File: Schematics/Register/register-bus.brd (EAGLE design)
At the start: 119.4 x 70.8 mm, 17 parts

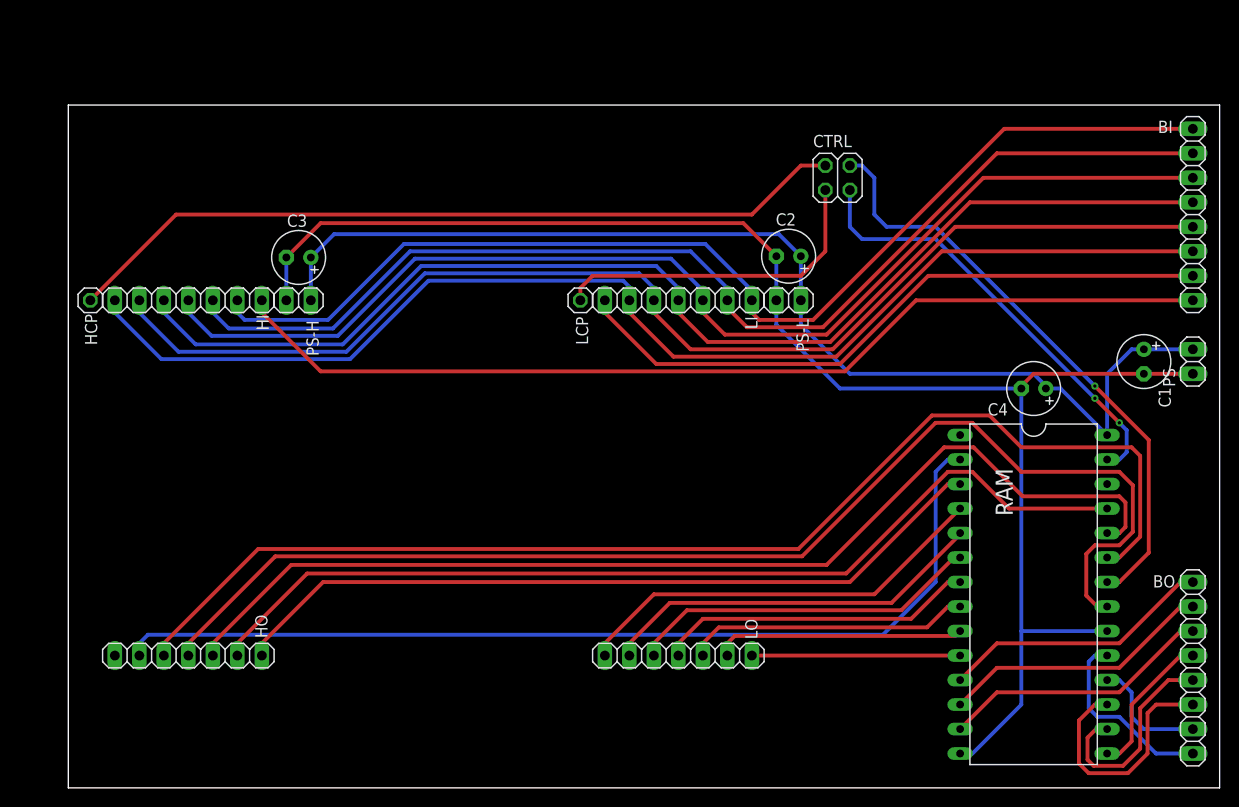
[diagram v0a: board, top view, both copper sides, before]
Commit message: Register and RAM modules.
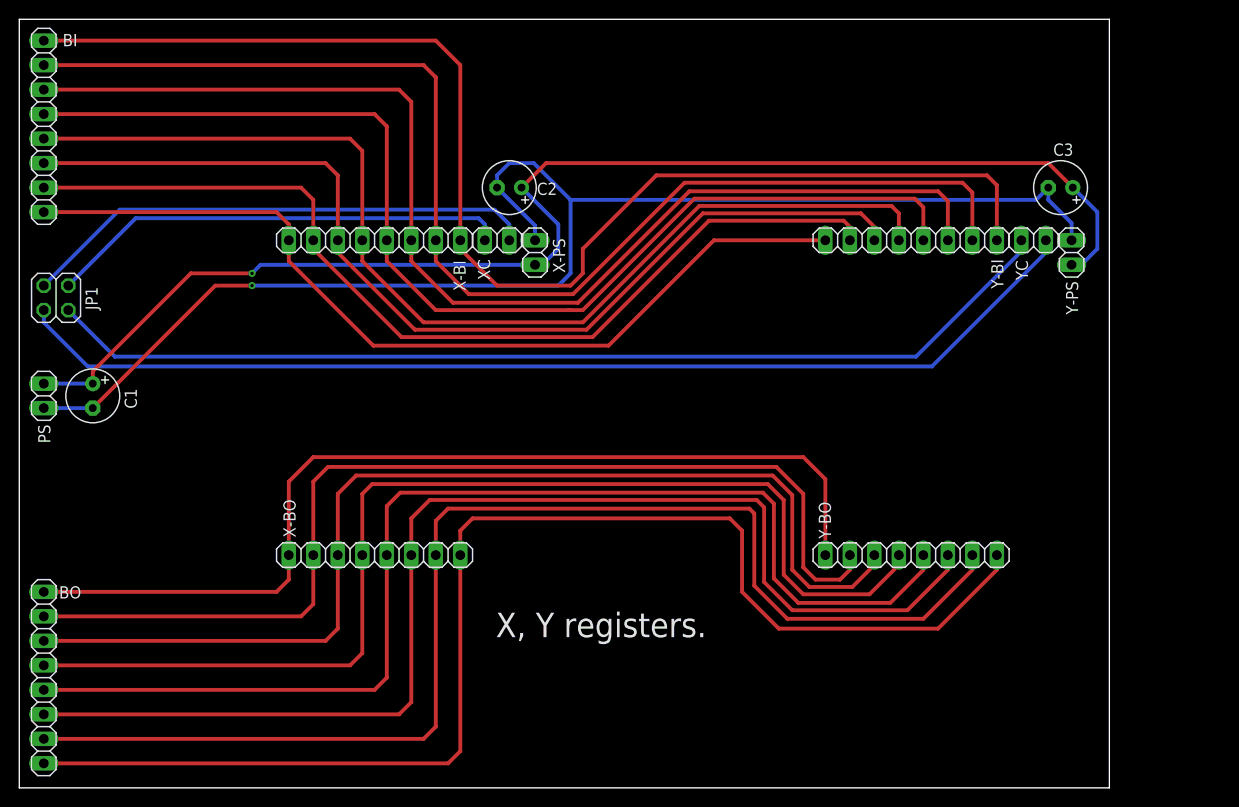
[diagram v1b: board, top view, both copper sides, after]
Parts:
- removed C4: (no value), rcl:E2,5-6
- removed CTRL: (no value), pinhead:2X02
- removed HCP, LCP: (no value), pinhead:1X01
- removed HI, HO, LI, LO: (no value), pinhead:1X07
- removed PS-H, PS-L: (no value), pinhead:1X02
- removed RAM: AT28C64B, memory-nec:DIL28-6
- added JP1: (no value), pinhead:2X02
- added X-BI, X-BO, Y-BI, Y-BO: (no value), pinhead:1X08
- added X-PS, XC, Y-PS, YC: (no value), pinhead:1X02
- moved BI 119.5 mm to (-2.54, 68.6)
- moved PS 119.2 mm to (-2.54, 40.6)
- moved BO 119.1 mm to (-2.54, 11.4)
- moved C1 109.0 mm to (2.54, 40.6)
- moved C3 79.3 mm to (102.9, 62.2)
- moved C2 29.8 mm to (45.7, 62.2)
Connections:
- removed net A0: LO.7, RAM.10
- removed net A1: LO.6, RAM.9
- removed net A10: HO.4, RAM.21
- removed net A11: HO.3, RAM.23
- removed net A12: HO.2, RAM.2
- removed net A2: LO.5, RAM.8
- removed net A3: LO.4, RAM.7
- removed net A4: LO.3, RAM.6
- removed net A5: LO.2, RAM.5
- removed net A6: LO.1, RAM.4
- removed net A7: HO.7, RAM.3
- removed net A8: HO.6, RAM.25
- removed net A9: HO.5, RAM.24
- removed net B0: BI.8, HI.6, LI.7
- removed net B1: BI.7, HI.5, LI.6
- removed net B2: BI.6, HI.4, LI.5
- removed net B3: BI.5, HI.3, LI.4
- removed net B4: BI.4, HI.2, LI.3
- removed net B5: BI.3, HI.1, LI.2
- removed net B6: BI.2, LI.1
- removed net B7: BI.1, HI.7
- removed net HCP: CTRL.2, HCP.1
- removed net LCP: CTRL.1, LCP.1
- removed net O0: BO.8, RAM.11
- removed net O1: BO.7, RAM.12
- removed net O2: BO.6, RAM.13
- removed net O3: BO.5, RAM.15
- removed net O4: BO.4, RAM.16
- removed net O5: BO.3, RAM.17
- removed net O6: BO.2, RAM.18
- removed net O7: BO.1, RAM.19
- removed net OE: CTRL.4, RAM.22
- removed net WE: CTRL.3, RAM.27
- new net D0: BI.8, X-BI.1, Y-BI.1
- new net D1: BI.7, X-BI.2, Y-BI.2
- new net D2: BI.6, X-BI.3, Y-BI.3
- new net D3: BI.5, X-BI.4, Y-BI.4
- new net D4: BI.4, X-BI.5, Y-BI.5
- new net D5: BI.3, X-BI.6, Y-BI.6
- new net D6: BI.2, X-BI.7, Y-BI.7
- new net D7: BI.1, X-BI.8, Y-BI.8
- new net Q0: BO.8, X-BO.1, Y-BO.1
- new net Q1: BO.7, X-BO.2, Y-BO.2
- new net Q2: BO.6, X-BO.3, Y-BO.3
- new net Q3: BO.5, X-BO.4, Y-BO.4
- new net Q4: BO.4, X-BO.5, Y-BO.5
- new net Q5: BO.3, X-BO.6, Y-BO.6
- new net Q6: BO.2, X-BO.7, Y-BO.7
- new net Q7: BO.1, X-BO.8, Y-BO.8
- new net XCP: JP1.1, XC.2
- new net XOE: JP1.3, XC.1
- new net YCP: JP1.2, YC.2
- new net YOE: JP1.4, YC.1
- net GND: now also X-PS.2, Y-PS.2; no longer C4.-, PS-H.2, PS-L.2, RAM.14, RAM.20
- net VCC: now also X-PS.1, Y-PS.1; no longer C4.+, PS-H.1, PS-L.1, RAM.28
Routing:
- net Q7: track 0.00 -> 135.2 mm
- net D0: track 0.00 -> 132.8 mm
- net Q6: track 0.00 -> 131.4 mm
- net A10: track 128.9 -> 0.00 mm
- net B5: track 127.7 -> 0.00 mm
- net D1: track 0.00 -> 127.4 mm
- net A11: track 126.7 -> 0.00 mm
- net Q5: track 0.00 -> 126.6 mm
- net B4: track 125.6 -> 0.00 mm
- net B3: track 123.4 -> 0.00 mm
- net Q4: track 0.00 -> 122.3 mm
- net D2: track 0.00 -> 121.8 mm
- net B2: track 121.1 -> 0.00 mm
- net B1: track 118.8 -> 0.00 mm
- net Q3: track 0.00 -> 117.7 mm
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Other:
- board size 119.4 x 70.8 mm -> 113 x 79.7 mm
- board text added: "X, Y registers."
